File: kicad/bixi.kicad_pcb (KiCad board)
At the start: 2 copper layers, 100 x 100 mm, 34 parts, among them CON1 BARREL_JACK, J1 RJ45, J2 RJ45, J3 RJ45, J4 RJ45, J5 RJ45, J6 RJ45, J7 RJ45, J8 RJ45, U1 Teensy3.6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

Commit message: kicad schematic and layout
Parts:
- added REF**: 1pin, Connectors:1pin, F.Cu at (182.0, 120.5)
- added REF**: 1pin, Connectors:1pin, F.Cu at (108.8, 86.8)
- moved R1 46.3 mm to (116.0, 138.0)
- moved R4 43.0 mm to (176.0, 138.0)
- moved C5 39.9 mm to (173.0, 136.5), turned to 270 degrees
- moved R5 39.4 mm to (183.5, 87.0), turned to 180 degrees
- moved C4 39.1 mm to (113.0, 88.5), turned to 90 degrees
- moved R2 35.3 mm to (136.0, 138.0)
- moved C7 35.1 mm to (133.0, 136.5), turned to 270 degrees
- moved R3 33.8 mm to (156.0, 138.0)
- moved C6 31.8 mm to (153.0, 136.5), turned to 270 degrees
- moved R8 30.8 mm to (123.5, 87.0), turned to 180 degrees
- moved C8 29.5 mm to (173.0, 88.5), turned to 90 degrees
- moved R6 23.4 mm to (163.5, 87.0), turned to 180 degrees
- moved C2 22.6 mm to (133.0, 88.5), turned to 90 degrees
- moved C1 19.6 mm to (113.0, 136.5), turned to 270 degrees
- moved R7 18.7 mm to (143.5, 87.0), turned to 180 degrees
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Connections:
- U1 pad 53: Net-(U1-Pad53) -> VCC
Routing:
- net GND: track 0.00 -> 593.2 mm
- net VCC: track 0.00 -> 396.1 mm
- net /WS_5: track 0.00 -> 144.0 mm
- net /WS_2: track 0.00 -> 79.4 mm, vias 0 -> 3
- net /WS_8: track 0.00 -> 54.4 mm, vias 0 -> 1
- net /WS_7: track 0.00 -> 50.1 mm
- net /WS_4: track 0.00 -> 46.4 mm
- net /WS_6: track 0.00 -> 43.0 mm
- net Net-(J1-Pad1): track 0.00 -> 38.1 mm
- net /WS_3: track 0.00 -> 29.3 mm
- net Net-(J4-Pad1): track 0.00 -> 24.0 mm
- net Net-(J2-Pad1): track 0.00 -> 23.6 mm
- net Net-(J3-Pad1): track 0.00 -> 23.5 mm
- net Net-(J3-Pad2): track 0.00 -> 18.1 mm
- net Net-(J2-Pad2): track 0.00 -> 18.1 mm
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- removed copper zone on B.Cu, net GND
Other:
- board size 100 x 100 mm -> 82.6 x 100.3 mm
- net class Default: trace_width 0.25 -> 1; via_dia 0.6 -> 1; via_drill 0.4 -> 0.5

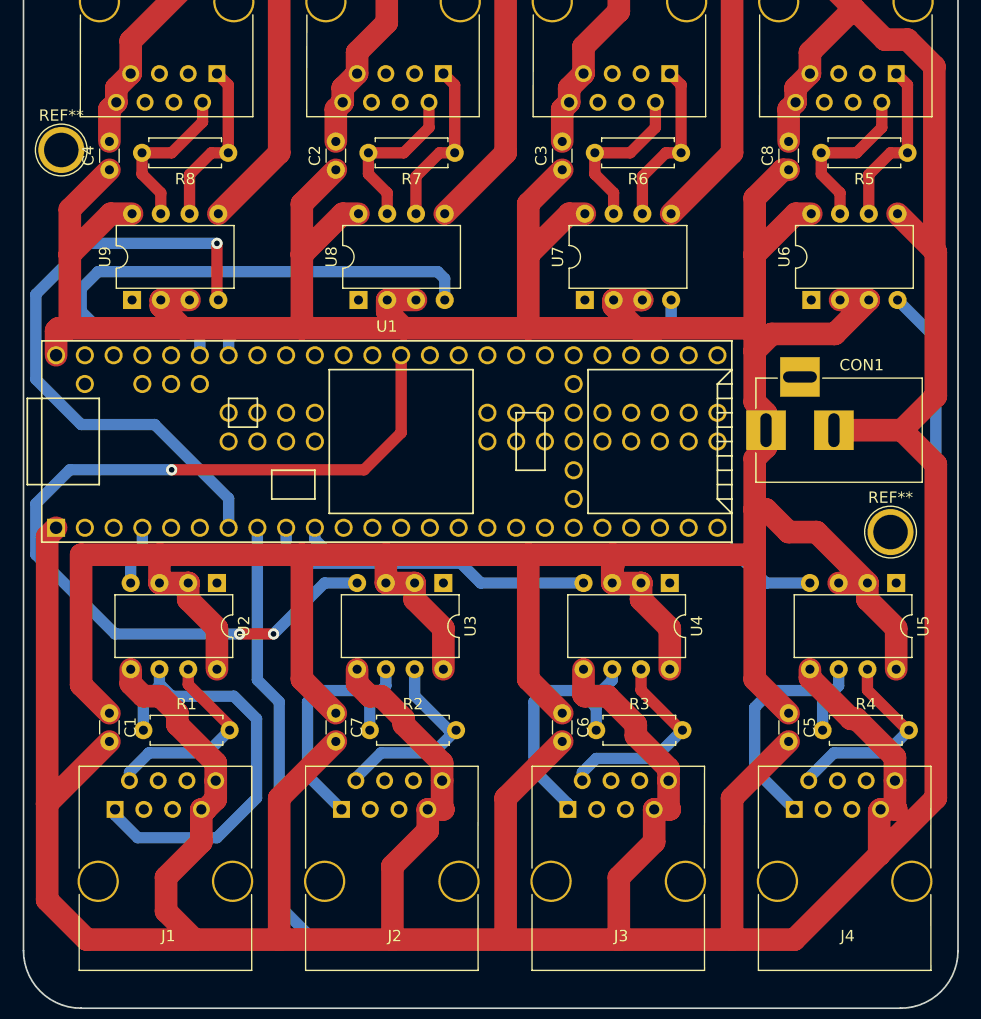
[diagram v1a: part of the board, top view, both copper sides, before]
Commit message: updated controller layout
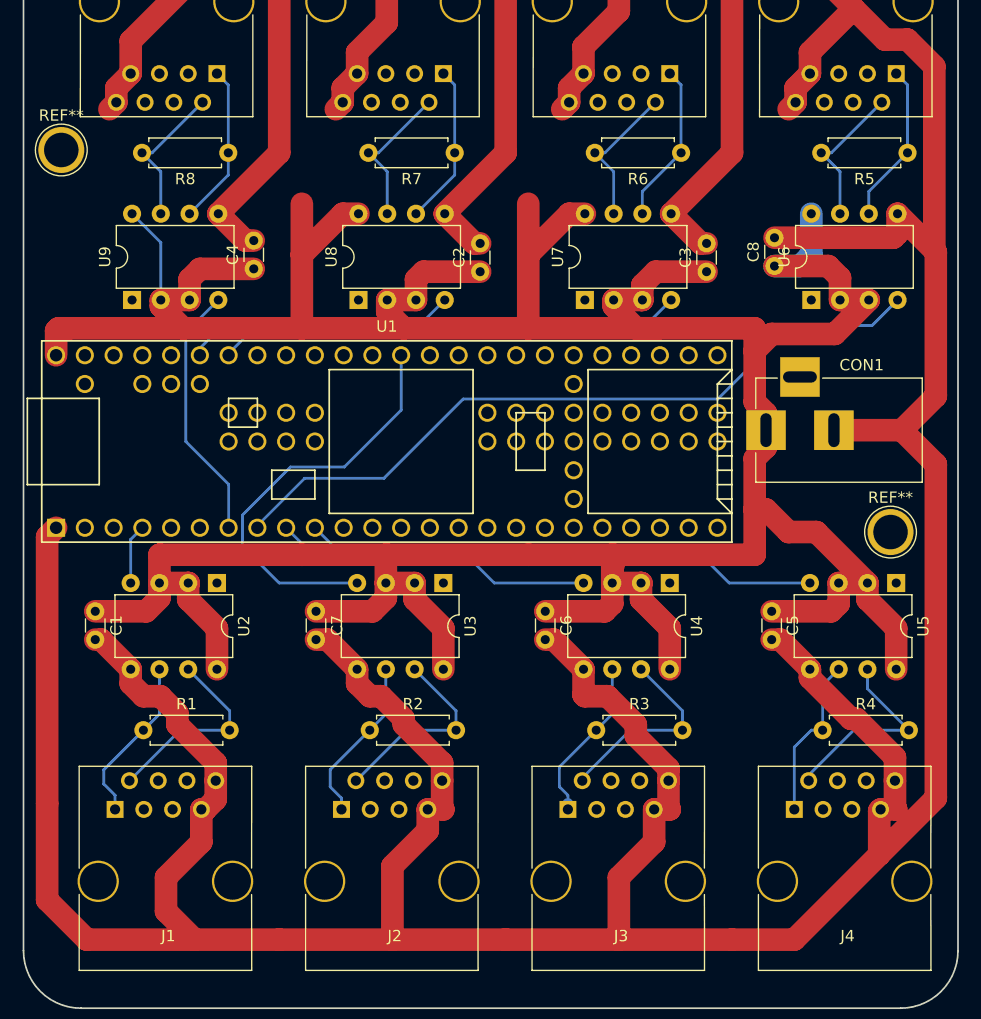
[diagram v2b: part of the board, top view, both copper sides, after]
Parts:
- moved C2 15.6 mm to (145.8, 97.5)
- moved C3 15.6 mm to (165.8, 97.5)
- moved C4 15.5 mm to (125.8, 97.2)
- moved C7 9.17 mm to (131.2, 127.5)
- moved C5 9.12 mm to (171.5, 127.5)
- moved C6 9.12 mm to (151.5, 127.5)
- moved C1 9.09 mm to (111.8, 127.5)
- moved C8 8.59 mm to (171.8, 97.0)
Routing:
- net /WS_5: track 144.0 -> 65.0 mm
- net /WS_2: track 79.4 -> 36.9 mm, vias 3 -> 0
- net VCC: track 396.1 -> 354.2 mm
- net GND: track 593.2 -> 558.5 mm
- net /WS_8: track 54.4 -> 22.9 mm, vias 1 -> 0
- net /WS_7: track 50.1 -> 24.0 mm
- net Net-(J1-Pad1): track 38.1 -> 14.8 mm
- net Net-(J4-Pad1): track 24.0 -> 14.6 mm
- net Net-(J2-Pad1): track 23.6 -> 14.8 mm
- net Net-(J3-Pad1): track 23.5 -> 15.1 mm
- net /WS_6: track 43.0 -> 41.2 mm
- net Net-(J6-Pad2): track 14.6 -> 13.3 mm
- net Net-(J5-Pad2): track 14.6 -> 13.3 mm
- net Net-(J7-Pad2): track 14.6 -> 13.3 mm
- net /WS_3: track 29.3 -> 28.3 mm
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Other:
- net class Default: trace_width 1 -> 2; via_dia 1 -> 0.5; via_drill 0.5 -> 0.4

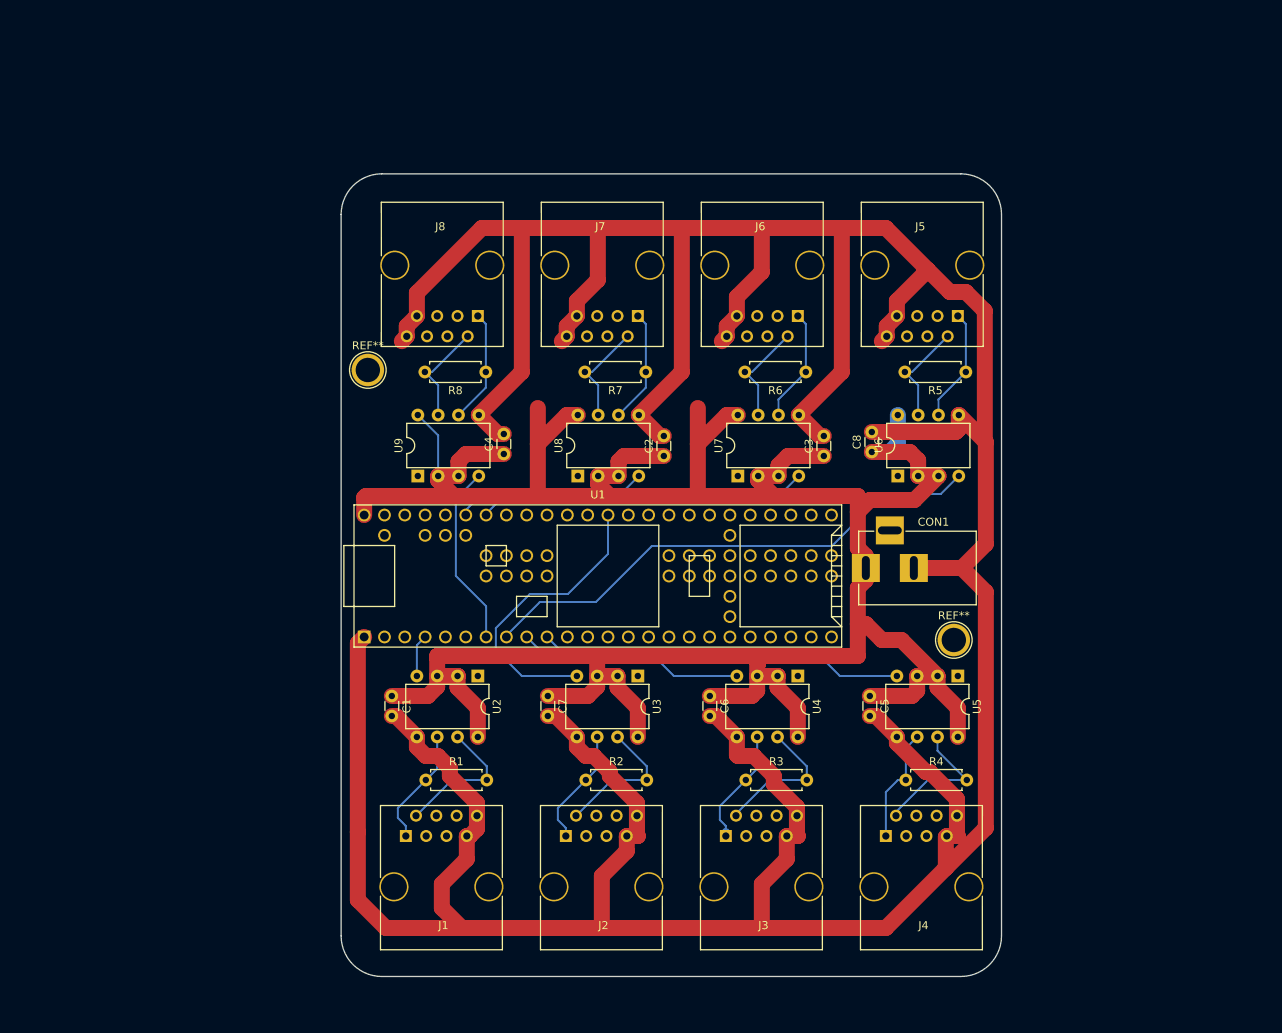
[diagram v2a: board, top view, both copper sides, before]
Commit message: more controller layout changes
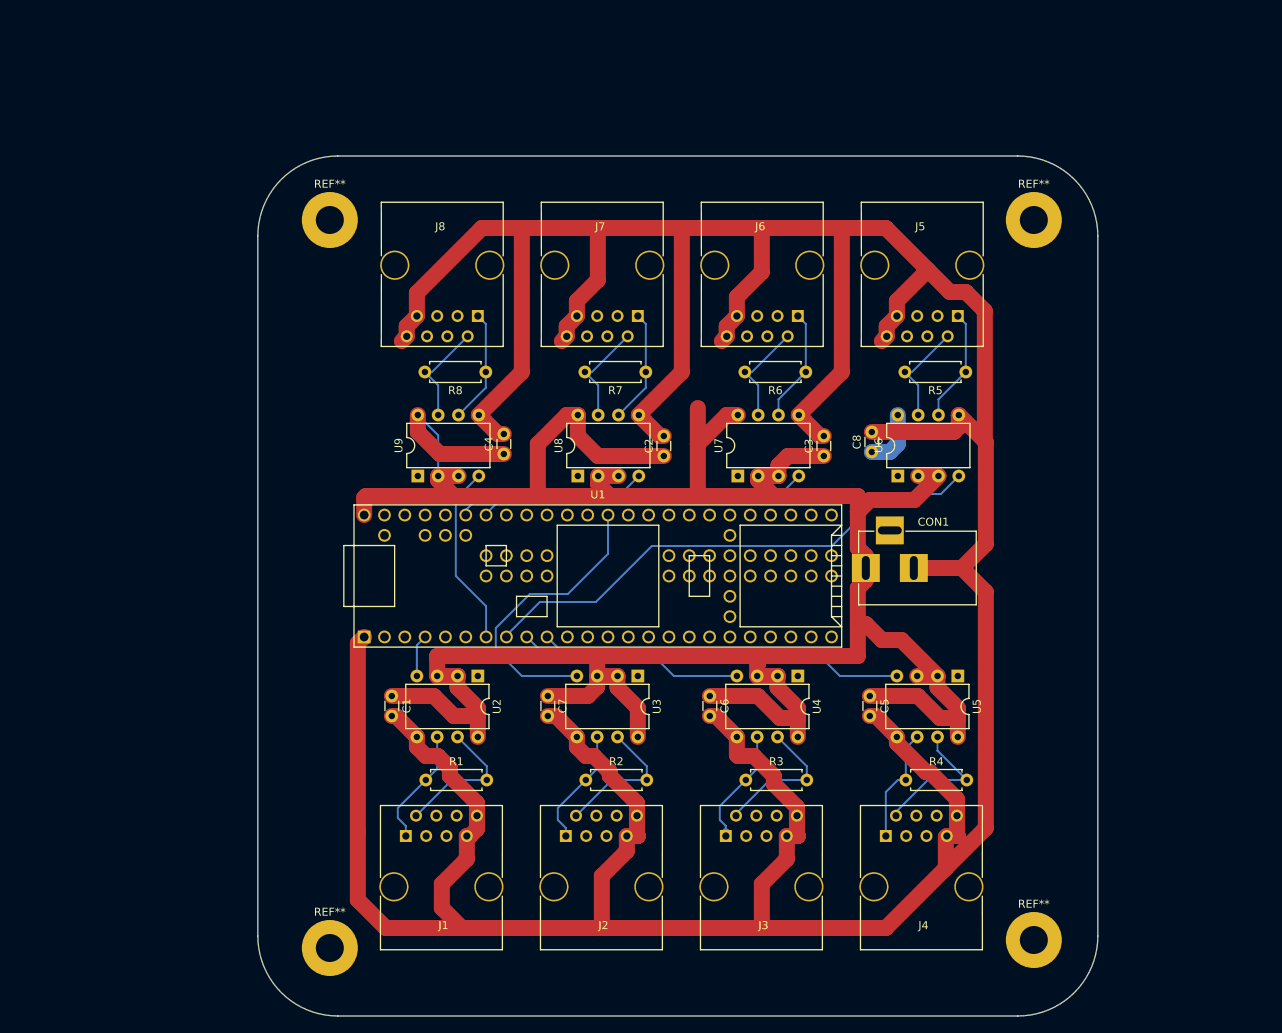
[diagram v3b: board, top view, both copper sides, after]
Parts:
- removed the REF** at (182.0, 120.5)
- removed the REF** at (108.8, 86.8)
- added REF**: MountingHole_3.5mm_Pad, Mounting_Holes:MountingHole_3.5mm_Pad, F.Cu at (192.0, 68.0)
- added REF**: MountingHole_3.5mm_Pad, Mounting_Holes:MountingHole_3.5mm_Pad, F.Cu at (104.0, 68.0)
- added REF**: MountingHole_3.5mm_Pad, Mounting_Holes:MountingHole_3.5mm_Pad, F.Cu at (104.0, 159.0)
- added REF**: MountingHole_3.5mm_Pad, Mounting_Holes:MountingHole_3.5mm_Pad, F.Cu at (192.0, 158.0)
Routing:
- net VCC: track 354.2 -> 366.8 mm
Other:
- board size 82.6 x 100.3 mm -> 105 x 107.5 mm

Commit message: controller and receiver boards almost done for v1
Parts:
- removed REF** (x4): MountingHole_3.5mm_Pad, Mounting_Holes:MountingHole_3.5mm_Pad
- C1, C2, C3, C4, C5, C6, C7, C8: footprint Capacitors_THT:C_Disc_D3.0mm_W1.6mm_P2.50mm -> Capacitors_THT:C_Disc_D3_P2.5
- R1, R2, R3, R4, R5, R6, R7, R8: footprint Resistors_THT:R_Axial_DIN0207_L6.3mm_D2.5mm_P7.62mm_Horizontal -> Resistors_THT:Resistor_Horizontal_RM7mm
- moved R1 20.2 mm to (106.0, 120.5)
- moved R2 20.2 mm to (126.0, 120.5)
- moved R3 20.2 mm to (146.0, 120.5)
- moved R4 20.2 mm to (166.0, 120.5)
- moved C1 19.0 mm to (104.2, 110.0)
- moved C2 19.0 mm to (138.2, 80.0)
- moved C3 19.0 mm to (158.2, 80.0)
- moved C4 19.0 mm to (118.2, 79.8)
- moved C5 19.0 mm to (164.0, 110.0)
- moved C6 19.0 mm to (144.0, 110.0)
- moved C7 19.0 mm to (123.8, 110.0)
- moved C8 19.0 mm to (164.2, 79.5)
- moved CON1 19.0 mm to (163.5, 94.0)
- moved J1 19.0 mm to (106.0, 127.5)
- moved J2 19.0 mm to (126.0, 127.5)
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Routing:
- net GND: track 558.3 -> 0.00 mm
- net VCC: track 366.8 -> 0.00 mm
- net /WS_2: track 36.9 -> 21.7 mm
- net Net-(J4-Pad2): track 17.9 -> 14.1 mm
- net Net-(J3-Pad2): track 17.7 -> 14.1 mm
- net Net-(J1-Pad2): track 17.6 -> 14.1 mm
- net Net-(J2-Pad2): track 17.6 -> 14.1 mm
- net /WS_8: track 22.9 -> 20.8 mm
- net Net-(J3-Pad1): track 15.1 -> 14.0 mm
- net Net-(J2-Pad1): track 14.8 -> 14.0 mm
- net Net-(J1-Pad1): track 14.8 -> 14.0 mm
- net /WS_5: track 65.0 -> 65.7 mm
- net /WS_4: track 45.8 -> 46.4 mm
- net Net-(J4-Pad1): track 14.6 -> 14.0 mm
- added copper zone on B.Cu, net GND
- added copper zone on F.Cu, net VCC
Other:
- board size 105 x 107.5 mm -> 87.5 x 100 mm
- net class Default: trace_width 2 -> 0.25

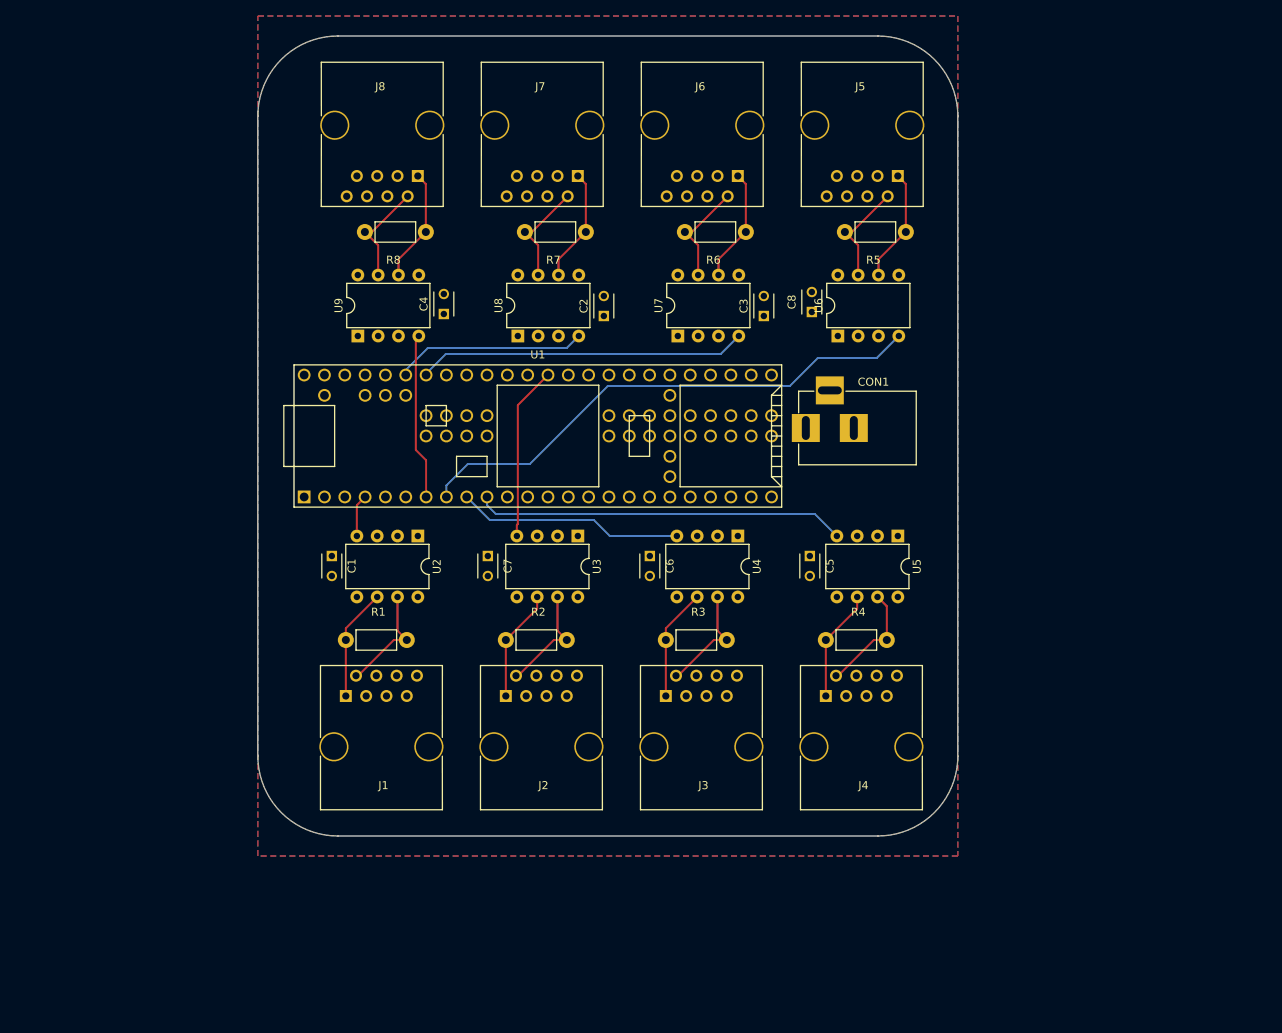
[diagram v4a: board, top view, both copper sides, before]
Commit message: controller board screw terminal, screw holes. ready for build
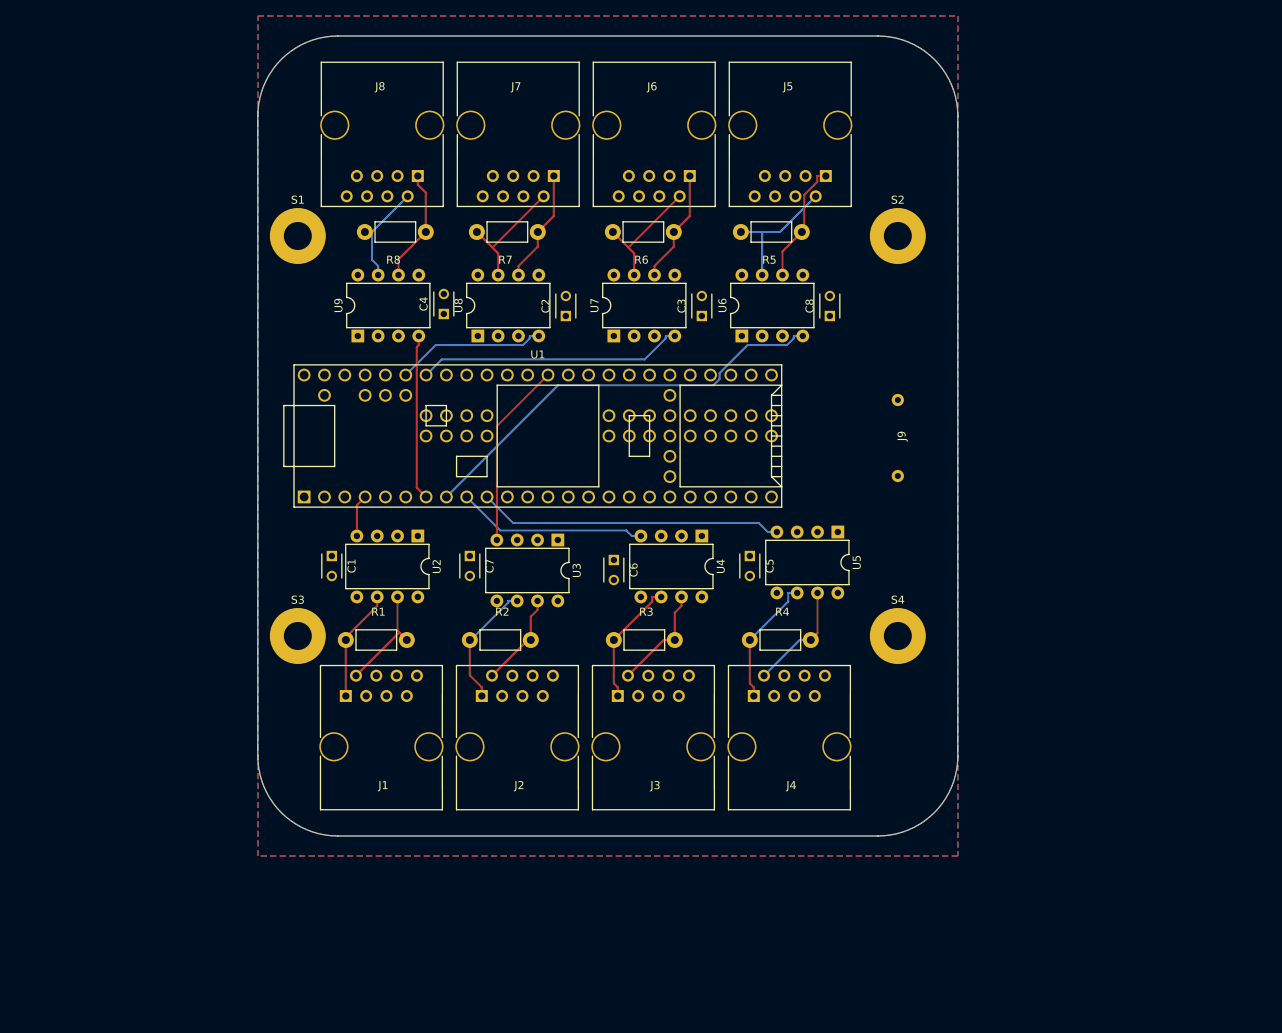
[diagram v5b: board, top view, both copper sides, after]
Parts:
- removed CON1: BARREL_JACK, Connectors:BARREL_JACK
- added J9: Screw_Terminal_1x02, custom:HB9500-2P, F.Cu at (175.0, 95.0)
- added S1: MountingHole_3.5mm_Pad, Mounting_Holes:MountingHole_3.5mm_Pad, F.Cu at (100.0, 70.0)
- added S2: MountingHole_3.5mm_Pad, Mounting_Holes:MountingHole_3.5mm_Pad, F.Cu at (175.0, 70.0)
- added S3: MountingHole_3.5mm_Pad, Mounting_Holes:MountingHole_3.5mm_Pad, F.Cu at (100.0, 120.0)
- added S4: MountingHole_3.5mm_Pad, Mounting_Holes:MountingHole_3.5mm_Pad, F.Cu at (175.0, 120.0)
- moved R5 13.0 mm to (163.0, 69.5)
- moved U6 12.0 mm to (155.5, 82.5)
- moved R4 9.50 mm to (156.5, 120.5)
- moved J4 9.00 mm to (157.0, 127.5)
- moved J5 9.00 mm to (166.0, 62.5)
- moved R6 9.00 mm to (147.0, 69.5)
- moved U7 8.00 mm to (139.5, 82.5)
- moved C3 7.75 mm to (150.5, 80.0)
- moved U5 7.52 mm to (167.5, 107.0)
- moved C5 7.50 mm to (156.5, 110.0)
- moved R3 6.50 mm to (139.5, 120.5)
- moved J3 6.00 mm to (140.0, 127.5)
- moved J6 6.00 mm to (149.0, 62.5)
- moved R7 6.00 mm to (130.0, 69.5)
- moved U8 5.00 mm to (122.5, 82.5)
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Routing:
- net /WS_5: track 65.7 -> 53.5 mm
- net /WS_4: track 46.4 -> 38.0 mm
- net /WS_6: track 41.2 -> 33.3 mm
- net /WS_7: track 24.0 -> 18.8 mm
- net /WS_3: track 28.3 -> 23.8 mm
- net Net-(J5-Pad2): track 13.3 -> 16.6 mm
- net Net-(J7-Pad2): track 13.3 -> 15.5 mm
- net Net-(J6-Pad2): track 13.3 -> 15.5 mm
- net Net-(J4-Pad1): track 14.0 -> 16.2 mm
- net Net-(J2-Pad2): track 14.1 -> 11.9 mm
- net Net-(J3-Pad1): track 14.0 -> 15.7 mm
- net Net-(J2-Pad1): track 14.0 -> 15.7 mm
- net /WS_2: track 21.7 -> 23.3 mm
- net Net-(J5-Pad1): track 14.2 -> 15.3 mm
- net Net-(J3-Pad2): track 14.1 -> 13.4 mm
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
